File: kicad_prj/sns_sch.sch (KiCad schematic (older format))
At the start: 54 parts

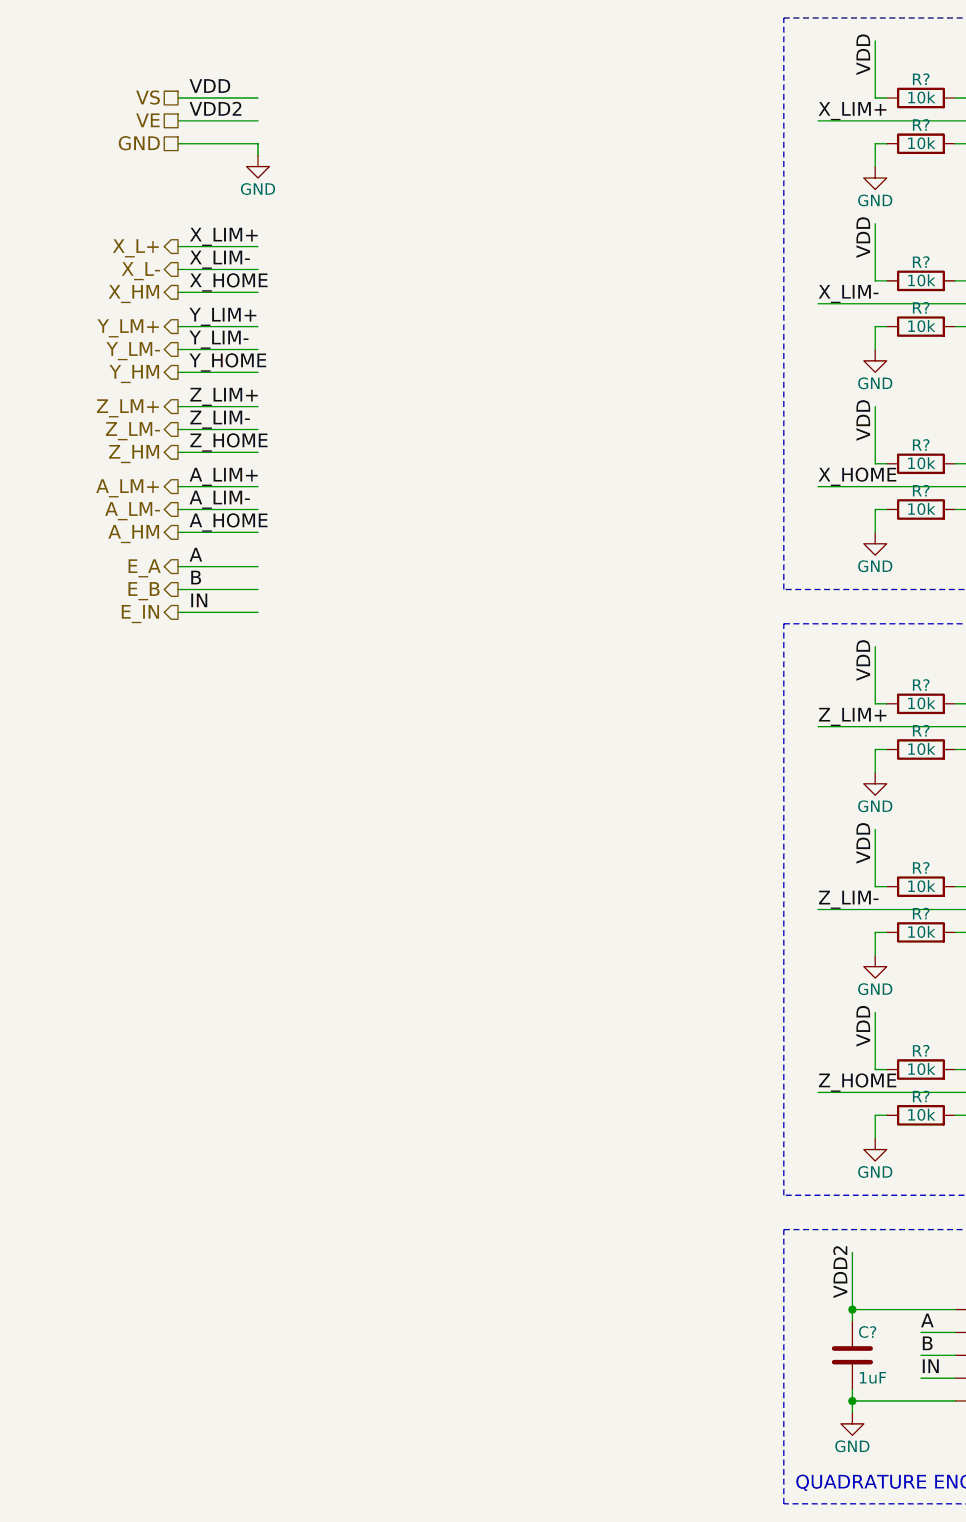
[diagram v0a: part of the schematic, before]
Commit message: Schematics 4
Finished sensor inputs.
Added DAC for stepper motor drivers.
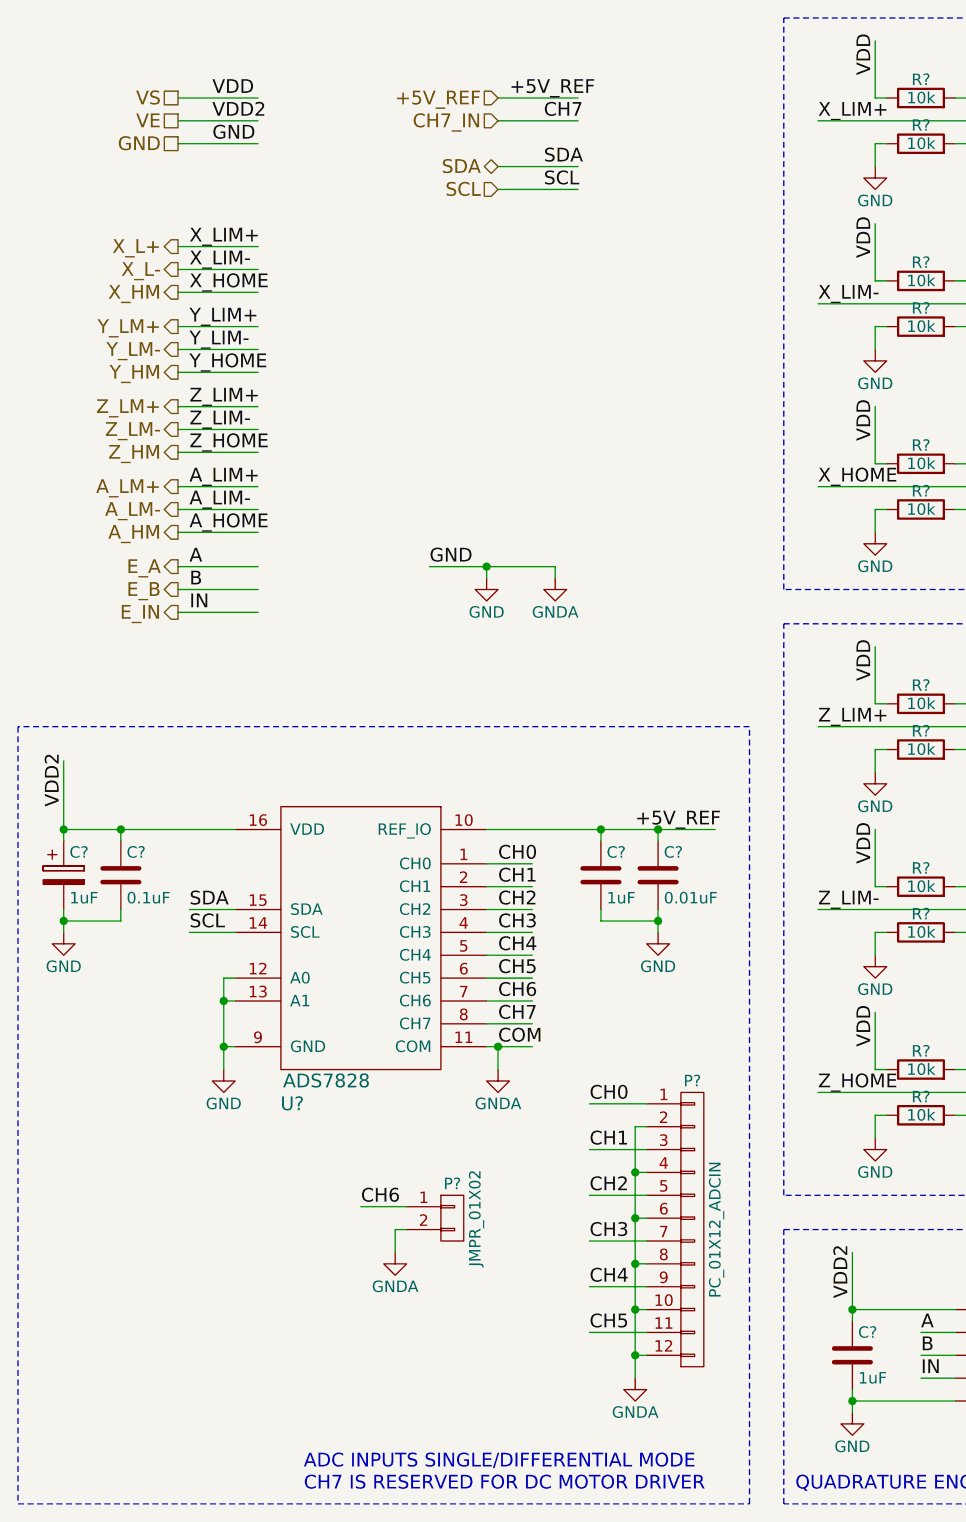
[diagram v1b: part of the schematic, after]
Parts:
- added C?: 1uF, symbol CP
- added C?: 0.1uF, symbol C
- added C?: 1uF, symbol C
- added C?: 0.01uF, symbol C
- added P?: JMPR_01X02, symbol JMPR_01X02
- added P?: PC_01X12_ADCIN, symbol PC_01X12_ADCIN
- added U?: ADS7828, symbol ADS7828
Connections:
- net labels added: +5V_REF, CH0, CH1, CH2, CH3, CH4, CH5, CH6, CH7, CH7_IN, COM, GNDA, SCL, SDA
- wire segments 186 -> 236
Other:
- note added: "ADC INPUTS SINGLE/DIFFERENTIAL MODE\nCH7 IS RESERVED FOR DC MOTOR DRIVER\n"

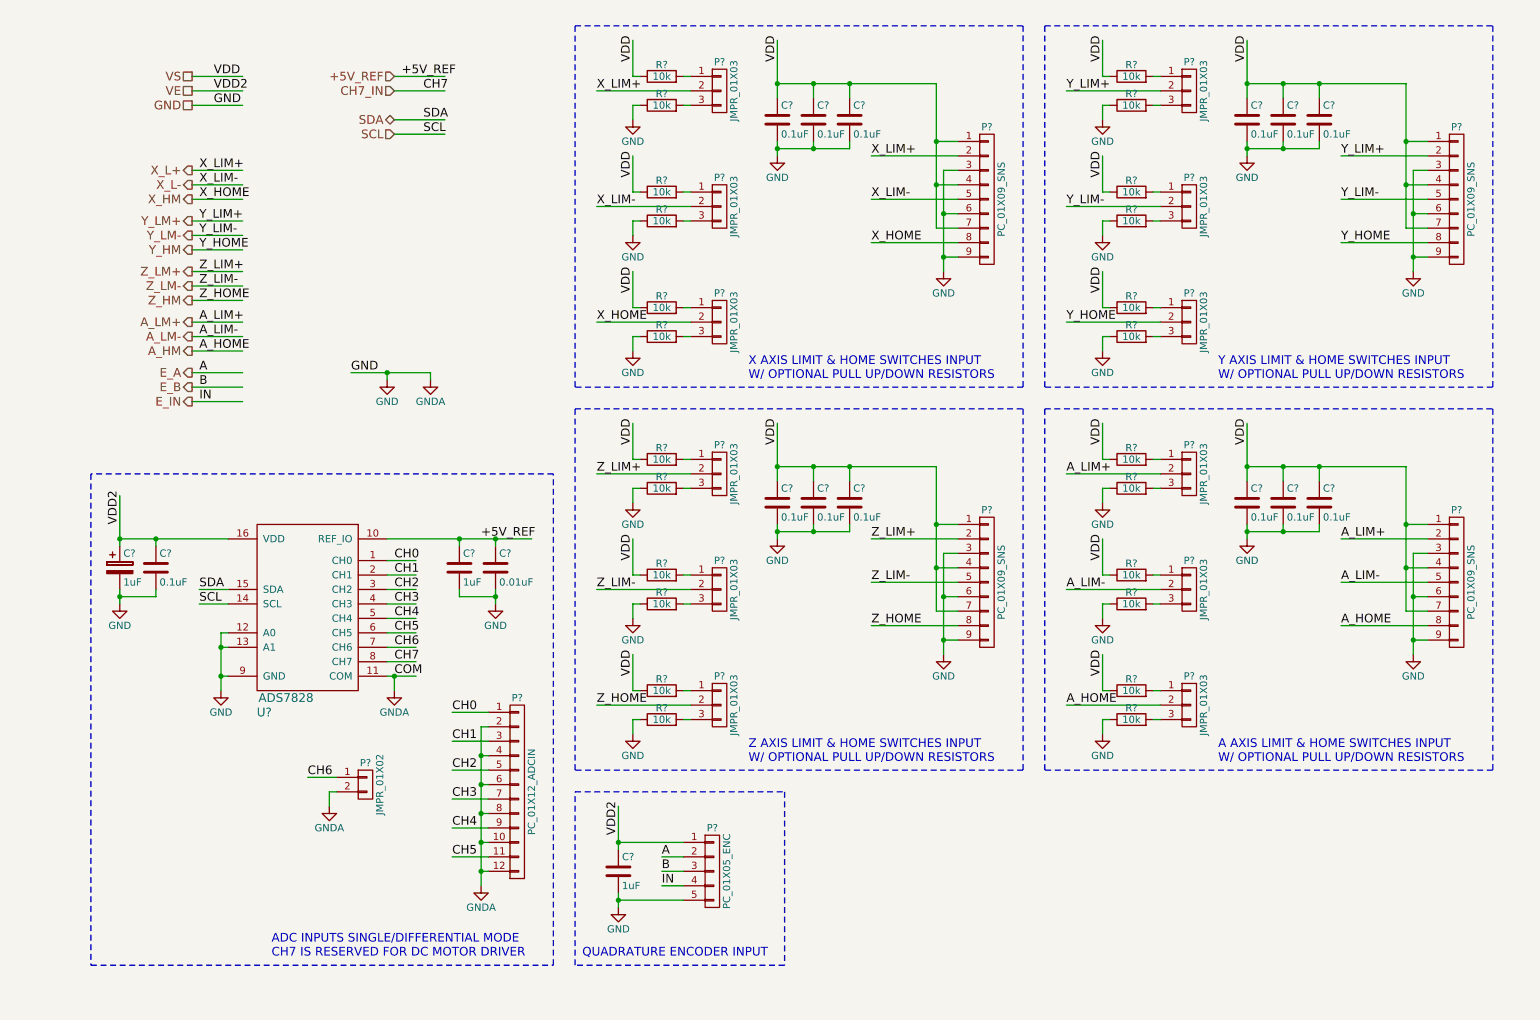
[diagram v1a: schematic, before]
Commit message: Schematics 5
Started isolation part.
Selected ICs for SPI isolation and general digital I/Os.
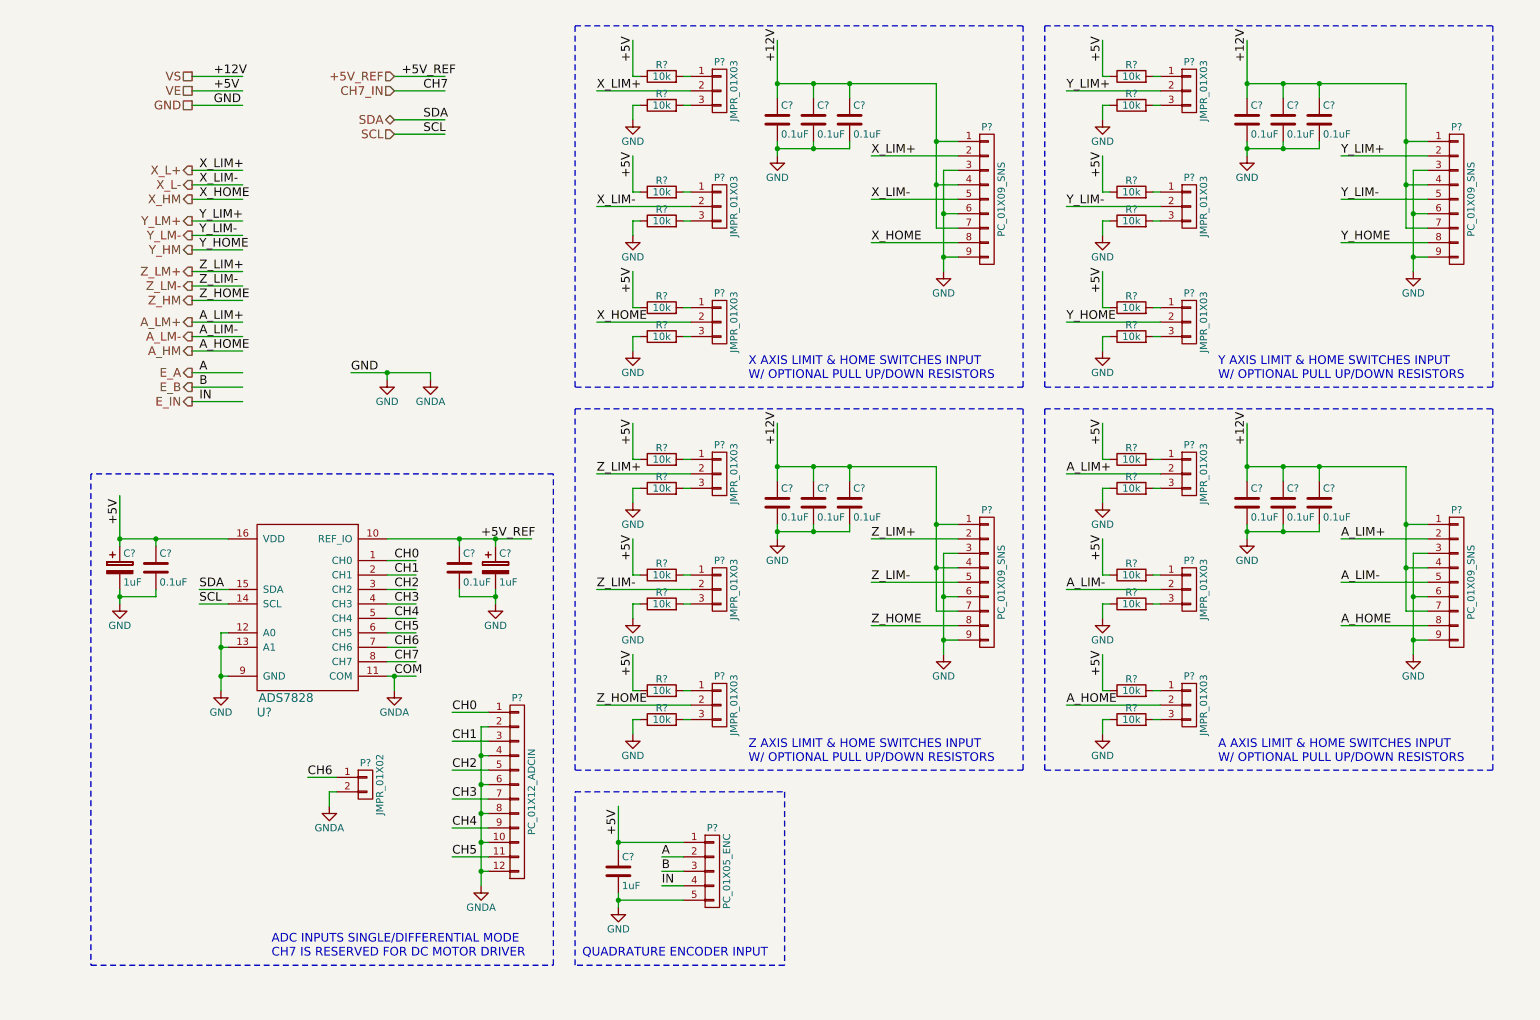
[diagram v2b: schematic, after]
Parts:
- removed C?: 1uF, symbol C
- added C?: 1uF, symbol CP
- C?: value 0.01uF -> 0.1uF
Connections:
- net labels added: +12V, +5V
- net labels removed: VDD, VDD2
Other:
- moved on the sheet: C?
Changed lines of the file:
@@
 $Descr A4 11693 8268
 encoding utf-8
-Sheet 7 8
+Sheet 7 9
 Title ""
 Date ""
@@
 $EndComp
 Text Label 6000 900  1    60   ~ 0
-VDD
++12V
 $Comp
 L JMPR_01X03 P?
@@
 $EndComp
 Text Label 5000 900  1    60   ~ 0
-VDD
++5V
 Text Label 4750 1100 0    60   ~ 0
 X_LIM+
@@
 $EndComp
 Text Label 5000 1700 1    60   ~ 0
-VDD
++5V
 Text Label 4750 1900 0    60   ~ 0
 X_LIM-
@@
 $EndComp
 Text Label 5000 2500 1    60   ~ 0
-VDD
++5V
 Text Label 4750 2700 0    60   ~ 0
 X_HOME
@@
 $EndComp
 Text Label 6000 3550 1    60   ~ 0
-VDD
++12V
 $Comp
 L JMPR_01X03 P?
@@
 $EndComp
 Text Label 5000 3550 1    60   ~ 0
-VDD
++5V
 Text Label 4750 3750 0    60   ~ 0
 Z_LIM+
@@
 $EndComp
 Text Label 5000 4350 1    60   ~ 0
-VDD
++5V
 Text Label 4750 4550 0    60   ~ 0
 Z_LIM-
@@
 $EndComp
 Text Label 5000 5150 1    60   ~ 0
-VDD
++5V
 Text Label 4750 5350 0    60   ~ 0
 Z_HOME
@@
 $EndComp
 Text Label 9250 900  1    60   ~ 0
-VDD
++12V
 $Comp
 L JMPR_01X03 P?
@@
 $EndComp
 Text Label 8250 900  1    60   ~ 0
-VDD
++5V
 Text Label 8000 1100 0    60   ~ 0
 Y_LIM+
@@
 $EndComp
 Text Label 8250 1700 1    60   ~ 0
-VDD
++5V
 Text Label 8000 1900 0    60   ~ 0
 Y_LIM-
@@
 $EndComp
 Text Label 8250 2500 1    60   ~ 0
-VDD
++5V
 Text Label 8000 2700 0    60   ~ 0
 Y_HOME
@@
 $EndComp
 Text Label 9250 3550 1    60   ~ 0
-VDD
++12V
 $Comp
 L JMPR_01X03 P?
@@
 $EndComp
 Text Label 8250 3550 1    60   ~ 0
-VDD
++5V
 Text Label 8000 3750 0    60   ~ 0
 A_LIM+
@@
 $EndComp
 Text Label 8250 4350 1    60   ~ 0
-VDD
++5V
 Text Label 8000 4550 0    60   ~ 0
 A_LIM-
@@
 $EndComp
 Text Label 8250 5150 1    60   ~ 0
-VDD
++5V
 Text Label 8000 5350 0    60   ~ 0
 A_HOME
@@
 IN
 Text Label 4900 6250 1    60   ~ 0
-VDD2
++5V
 $Comp
 L C C?
@@
 E_IN
 Text Label 2100 1000 0    60   ~ 0
-VDD
++12V
 Text Label 2100 1100 0    60   ~ 0
-VDD2
++5V
 Text Label 2000 1650 0    60   ~ 0
 X_LIM+
@@
 $EndComp
 Text Label 1450 4100 1    60   ~ 0
-VDD2
++5V
 $Comp
 L GND #PWR?
@@
 $Comp
 L C C?
-U 1 1 5657BB6A
+U 1 1 5657BC5E
 P 3800 4400
 F 0 "C?" H 3825 4500 50  0000 L CNN
-F 1 "1uF" H 3825 4300 50  0000 L CNN
+F 1 "0.1uF" H 3825 4300 50  0000 L CNN
 F 2 "" H 3838 4250 30  0000 C CNN
 F 3 "" H 3800 4400 60  0000 C CNN
 	1    3800 4400
-	1    0    0    -1
-$EndComp
-$Comp
-L C C?
-U 1 1 5657BC5E
-P 4050 4400
-F 0 "C?" H 4075 4500 50  0000 L CNN
-F 1 "0.01uF" H 4075 4300 50  0000 L CNN
-F 2 "" H 4088 4250 30  0000 C CNN
-F 3 "" H 4050 4400 60  0000 C CNN
-	1    4050 4400
 	1    0    0    -1
 $EndComp
@@
 Text Label 3550 1400 0    60   ~ 0
 SCL
+$Comp
+L CP C?
+U 1 1 565B5CFC
+P 4050 4400
+F 0 "C?" H 4075 4500 50  0000 L CNN
+F 1 "1uF" H 4075 4300 50  0000 L CNN
+F 2 "" H 4088 4250 30  0000 C CNN
+F 3 "" H 4050 4400 60  0000 C CNN
+	1    4050 4400
+	1    0    0    -1
+$EndComp
 $EndSCHEMATC

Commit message: Schematics 6
Added isolation.
Misc. i2c, I/Os, spi. Need to finish iso2 sheet.
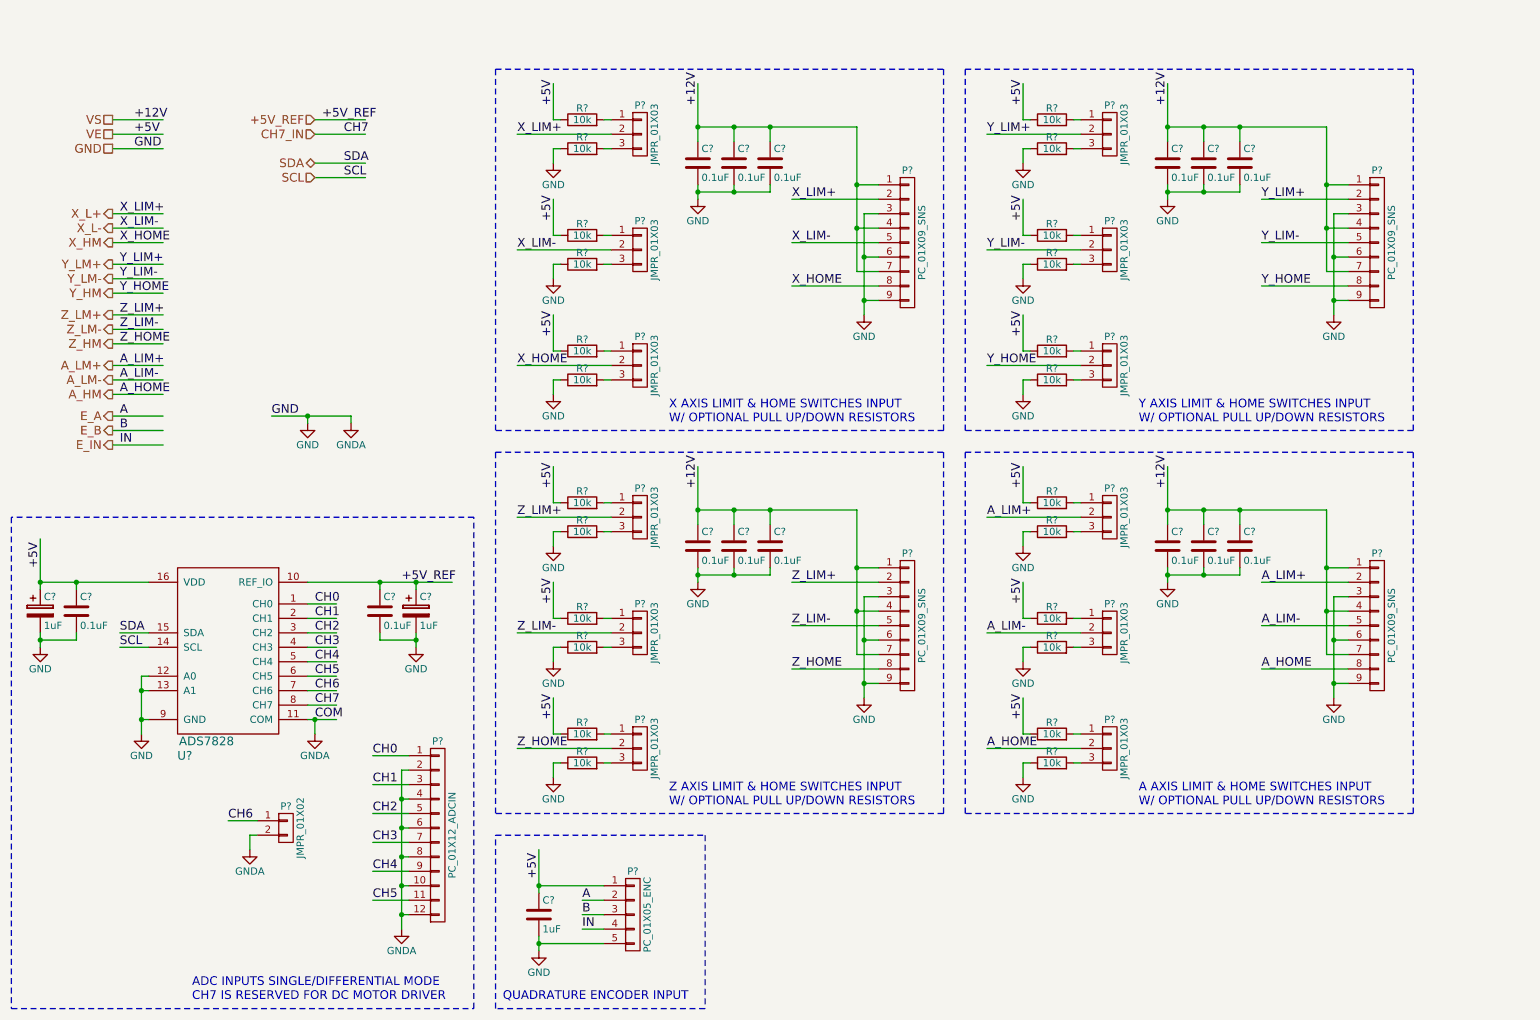
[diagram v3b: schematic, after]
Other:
- moved on the sheet: C?, P?, R?, U?
